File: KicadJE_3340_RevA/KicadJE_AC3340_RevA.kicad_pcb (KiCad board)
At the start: 2 copper layers, 200 x 128 mm, 146 parts, among them J101 RampOut1, J102 PulseOut2, J103 SawOut3, J104 In1.1, J105 In1.2, J106 In1.3, J107 SS_In2, J108 HS_In3, J109 FM_In4, J110 PWM_In5, J111 SineOut4, P101 HEADER_2x5_Doepfer, Q101 MMBT3906, Q102 UMX1N, SW101 Octave (3 state), U101 TL072, U102 TL072, U103 TL072, U104 AS3340, U105 L78L05_SOT89, U106 L79L05_SOT89, U107 TL072

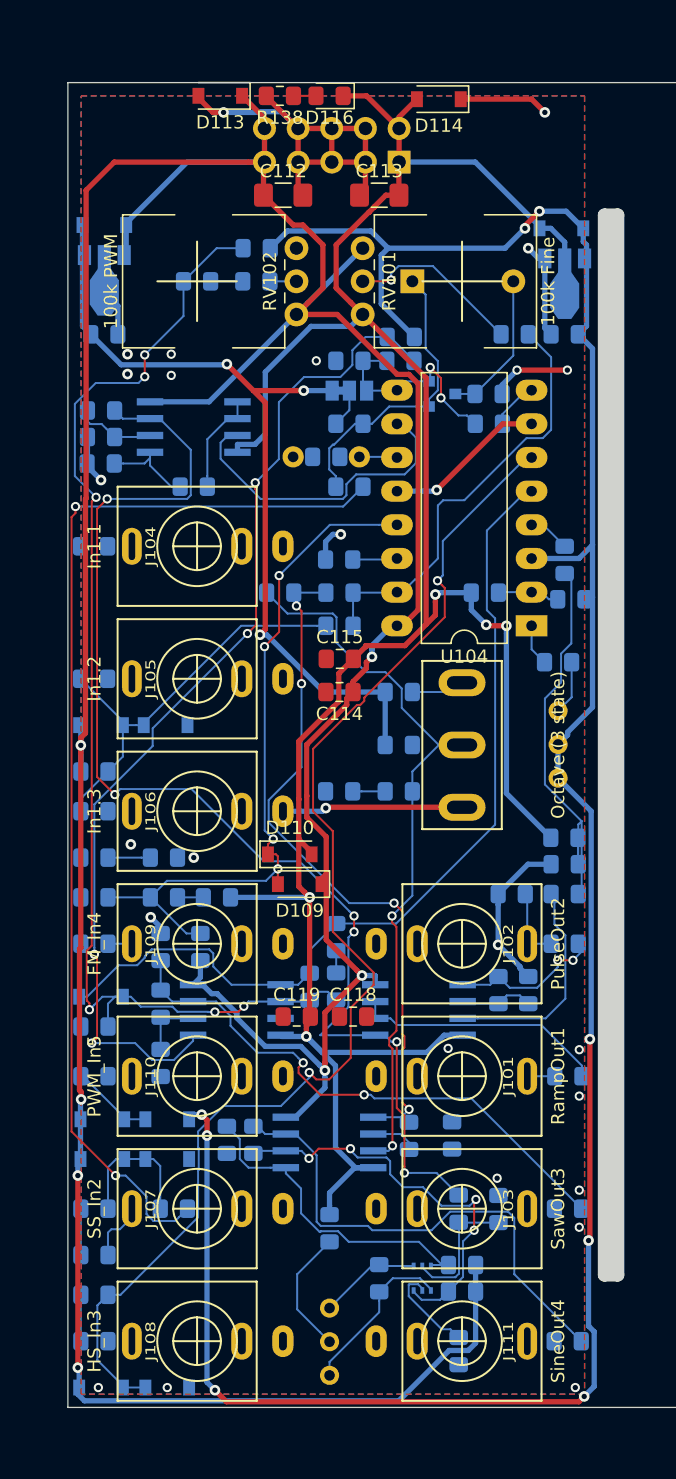
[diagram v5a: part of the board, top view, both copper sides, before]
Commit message: Update KicadJE_AC3340_RevA.kicad_pcb
DRC
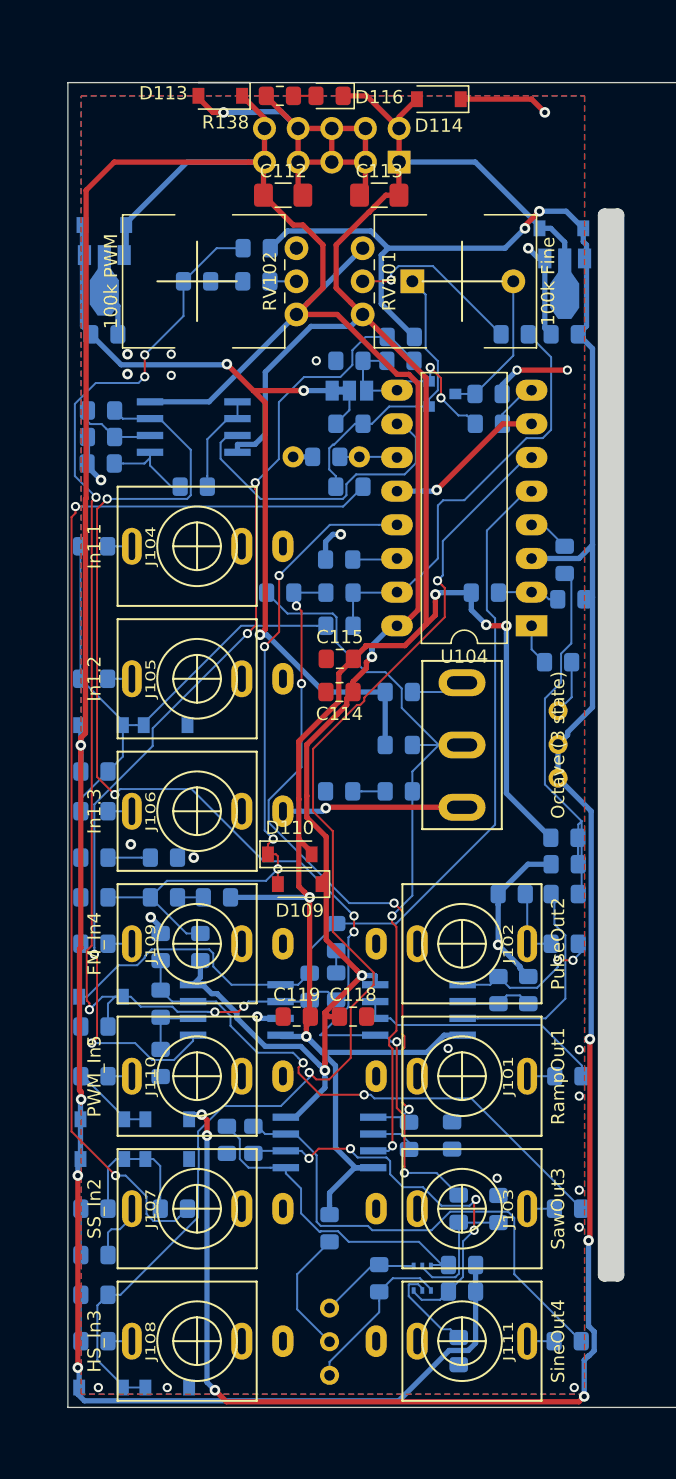
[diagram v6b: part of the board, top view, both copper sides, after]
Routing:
- net Net-(D103-Pad2): track 34.7 -> 44.7 mm
- net 3Octave: track 55.3 -> 59.1 mm
- net GND: track 105.1 -> 108.4 mm, vias 27 -> 28
- net Net-(J103-PadT): track 0.00 -> 2.05 mm
- net 3Sine: track 0.00 -> 2.03 mm
- net Net-(J105-PadT): track 0.00 -> 1.83 mm
- net Net-(J104-PadT): track 0.00 -> 1.83 mm
- net Net-(J110-PadT): track 0.00 -> 1.80 mm
- net Net-(J108-PadT): track 0.00 -> 1.80 mm
- net Net-(J106-PadT): track 0.00 -> 1.80 mm
- net Net-(C110-Pad2): track 2.86 -> 4.34 mm
- net +12VA: track 295.9 -> 297.1 mm
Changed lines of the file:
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@@
     (thickness 1.6)
     (drawings 122)
-    (tracks 956)
+    (tracks 978)
     (zones 0)
     (modules 146)
@@
     (tags SOD-123)
     (attr smd)
-    (fp_text reference D113 (at 0 -2 180) (layer F.SilkS)
+    (fp_text reference D113 (at 4.3 0.2 180) (layer F.SilkS)
       (effects (font (size 1 1) (thickness 0.15)))
     )
-    (fp_text value 1N1007 (at 0 2.1 180) (layer F.Fab)
+    (fp_text value 1N1007 (at 5.5 0.2 180) (layer F.Fab)
       (effects (font (size 1 1) (thickness 0.15)))
     )
@@
     (tags "LED handsolder")
     (attr smd)
-    (fp_text reference D116 (at 0 -1.65 180) (layer F.SilkS)
+    (fp_text reference D116 (at -3.75 -0.1 180) (layer F.SilkS)
       (effects (font (size 1 1) (thickness 0.15)))
     )
-    (fp_text value LED (at 0 1.65 180) (layer F.Fab)
+    (fp_text value LED (at -3.45 0.1 180) (layer F.Fab)
       (effects (font (size 1 1) (thickness 0.15)))
     )
@@
     (tags "resistor handsolder")
     (attr smd)
-    (fp_text reference R138 (at 0 -1.65 180) (layer F.SilkS)
+    (fp_text reference R138 (at 4.1 -2 180) (layer F.SilkS)
       (effects (font (size 1 1) (thickness 0.15)))
     )
-    (fp_text value 22k (at 0 1.65 180) (layer F.Fab)
+    (fp_text value 22k (at -0.1 0 180) (layer F.Fab)
       (effects (font (size 1 1) (thickness 0.15)))
     )
@@
   (via (at 57.8 70.5) (size 0.7) (drill 0.4) (layers F.Cu B.Cu) (net 1))
   (via (at 57.8 72.1) (size 0.7) (drill 0.4) (layers F.Cu B.Cu) (net 1))
-  (via (at 88.3 148.5) (size 0.7) (drill 0.4) (layers F.Cu B.Cu) (net 1))
   (via (at 52.3 148.5) (size 0.7) (drill 0.4) (layers F.Cu B.Cu) (net 1))
   (via (at 57.5 148.5) (size 0.7) (drill 0.4) (layers F.Cu B.Cu) (net 1))
@@
   (segment (start 82.475 115.081359) (end 82.475 112.05) (width 0.4) (layer B.Cu) (net 1))
   (via (at 82.475 115.081359) (size 0.8) (drill 0.4) (layers F.Cu B.Cu) (net 1))
+  (via (at 88.221743 148.5) (size 0.7) (drill 0.4) (layers F.Cu B.Cu) (net 1))
+  (segment (start 67 78.25) (end 68.475 78.25) (width 0.4) (layer B.Cu) (net 1))
+  (via (at 64.3 120.5) (size 0.8) (drill 0.4) (layers F.Cu B.Cu) (net 1))
+  (segment (start 66.05 120.635) (end 64.435 120.635) (width 0.4) (layer B.Cu) (net 1))
+  (segment (start 64.435 120.635) (end 64.3 120.5) (width 0.4) (layer B.Cu) (net 1))
   (segment (start 54.83 115) (end 53.025 115) (width 0.15) (layer B.Cu) (net 2))
   (segment (start 50.975 114.2) (end 50.975 111.5) (width 0.15) (layer B.Cu) (net 3))
@@
   (segment (start 74.79 78.25) (end 74.84 78.3) (width 0.15) (layer B.Cu) (net 16))
   (segment (start 72 78.25) (end 74.79 78.25) (width 0.15) (layer B.Cu) (net 16))
+  (segment (start 70.525 78.25) (end 72 78.25) (width 0.15) (layer B.Cu) (net 16))
   (segment (start 64.84 53.46) (end 64.84 56) (width 0.4) (layer F.Cu) (net 17) (status 30))
   (segment (start 64.7625 56.0775) (end 64.84 56) (width 0.4) (layer F.Cu) (net 17) (status 30))
@@
   (segment (start 51.374999 81.378234) (end 51.374999 58.125001) (width 0.4) (layer F.Cu) (net 17))
   (segment (start 50.975 100.025) (end 50.975 99.459315) (width 0.4) (layer F.Cu) (net 17))
+  (segment (start 69.69998 120.5) (end 69.39999 120.20001) (width 0.4) (layer F.Cu) (net 17))
+  (segment (start 70.5 120.5) (end 69.69998 120.5) (width 0.4) (layer F.Cu) (net 17))
   (segment (start 51.1 68.375) (end 51.725 69) (width 0.4) (layer B.Cu) (net 18))
   (segment (start 51.1 60.75) (end 51.1 68.375) (width 0.4) (layer B.Cu) (net 18))
@@
   (segment (start 89.4 137.3) (end 89.3 137.4) (width 0.4) (layer F.Cu) (net 19))
   (via (at 88.971753 149.171753) (size 0.8) (drill 0.4) (layers F.Cu B.Cu) (net 19))
-  (segment (start 89.72501 148.418496) (end 88.971753 149.171753) (width 0.4) (layer B.Cu) (net 19))
-  (segment (start 89.72501 144.280754) (end 89.72501 148.418496) (width 0.4) (layer B.Cu) (net 19))
-  (segment (start 89.3 137.4) (end 89.3 143.855744) (width 0.4) (layer B.Cu) (net 19))
-  (segment (start 89.3 143.855744) (end 89.72501 144.280754) (width 0.4) (layer B.Cu) (net 19))
   (via (at 61.1 148.700001) (size 0.8) (drill 0.4) (layers F.Cu B.Cu) (net 19))
   (segment (start 61.971751 149.571752) (end 61.1 148.700001) (width 0.4) (layer F.Cu) (net 19))
@@
   (segment (start 59.5 127.9) (end 59.15 128.25) (width 0.4) (layer B.Cu) (net 19))
   (segment (start 60.1 127.9) (end 59.5 127.9) (width 0.4) (layer B.Cu) (net 19))
+  (segment (start 88.971753 146.428247) (end 88.971753 149.171753) (width 0.4) (layer B.Cu) (net 19))
+  (segment (start 89.29999 146.10001) (end 88.971753 146.428247) (width 0.4) (layer B.Cu) (net 19))
+  (segment (start 89.3 137.4) (end 89.3 143.855744) (width 0.4) (layer B.Cu) (net 19))
+  (segment (start 89.3 143.855744) (end 89.72501 144.280754) (width 0.4) (layer B.Cu) (net 19))
+  (segment (start 89.72501 144.280754) (end 89.72501 145.719246) (width 0.4) (layer B.Cu) (net 19))
+  (segment (start 89.72501 145.719246) (end 89.344246 146.10001) (width 0.4) (layer B.Cu) (net 19))
+  (segment (start 89.344246 146.10001) (end 89.29999 146.10001) (width 0.4) (layer B.Cu) (net 19))
+  (segment (start 86.725 135) (end 84.67 135) (width 0.15) (layer B.Cu) (net 27))
+  (segment (start 53.675 85) (end 54.83 85) (width 0.15) (layer B.Cu) (net 28))
+  (segment (start 53 85) (end 53.675 85) (width 0.15) (layer B.Cu) (net 28))
+  (segment (start 53.93 95) (end 53 95) (width 0.15) (layer B.Cu) (net 29))
+  (segment (start 54.83 95) (end 53.93 95) (width 0.15) (layer B.Cu) (net 29))
+  (segment (start 53.025 105) (end 54.83 105) (width 0.15) (layer B.Cu) (net 30))
+  (segment (start 53.025 145) (end 54.83 145) (width 0.15) (layer B.Cu) (net 32))
+  (segment (start 53.025 125) (end 54.83 125) (width 0.15) (layer B.Cu) (net 33))
+  (segment (start 85.57 145) (end 86.7 145) (width 0.15) (layer B.Cu) (net 34))
+  (segment (start 84.67 145) (end 85.57 145) (width 0.15) (layer B.Cu) (net 34))
+  (segment (start 76 100) (end 79.75 100) (width 0.15) (layer B.Cu) (net 43))
   (segment (start 77.550001 63.850001) (end 74.955025 63.850001) (width 0.15) (layer B.Cu) (net 47))
   (segment (start 72.25 65) (end 74.3 65) (width 0.15) (layer F.Cu) (net 47))
@@
   (segment (start 55.725001 98.35) (end 63.075001 91) (width 0.15) (layer B.Cu) (net 71))
   (segment (start 55.725001 98.5) (end 55.725001 98.35) (width 0.15) (layer B.Cu) (net 71))
+  (segment (start 50.95 95) (end 50.95 85) (width 0.15) (layer B.Cu) (net 71))
   (segment (start 76.1 141.275) (end 76.1 141.175) (width 0.15) (layer B.Cu) (net 72) (status 30))
   (segment (start 76.698372 141.873372) (end 76.1 141.275) (width 0.15) (layer B.Cu) (net 72) (status 20))
